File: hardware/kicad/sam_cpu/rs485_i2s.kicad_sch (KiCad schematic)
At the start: 22 parts, among them J27 J27 RS485 IN, J28 J28 I2S IN, J29 J29 RS485 OUT, J30 J30 LINE IN, U32 CA-IS2092VW

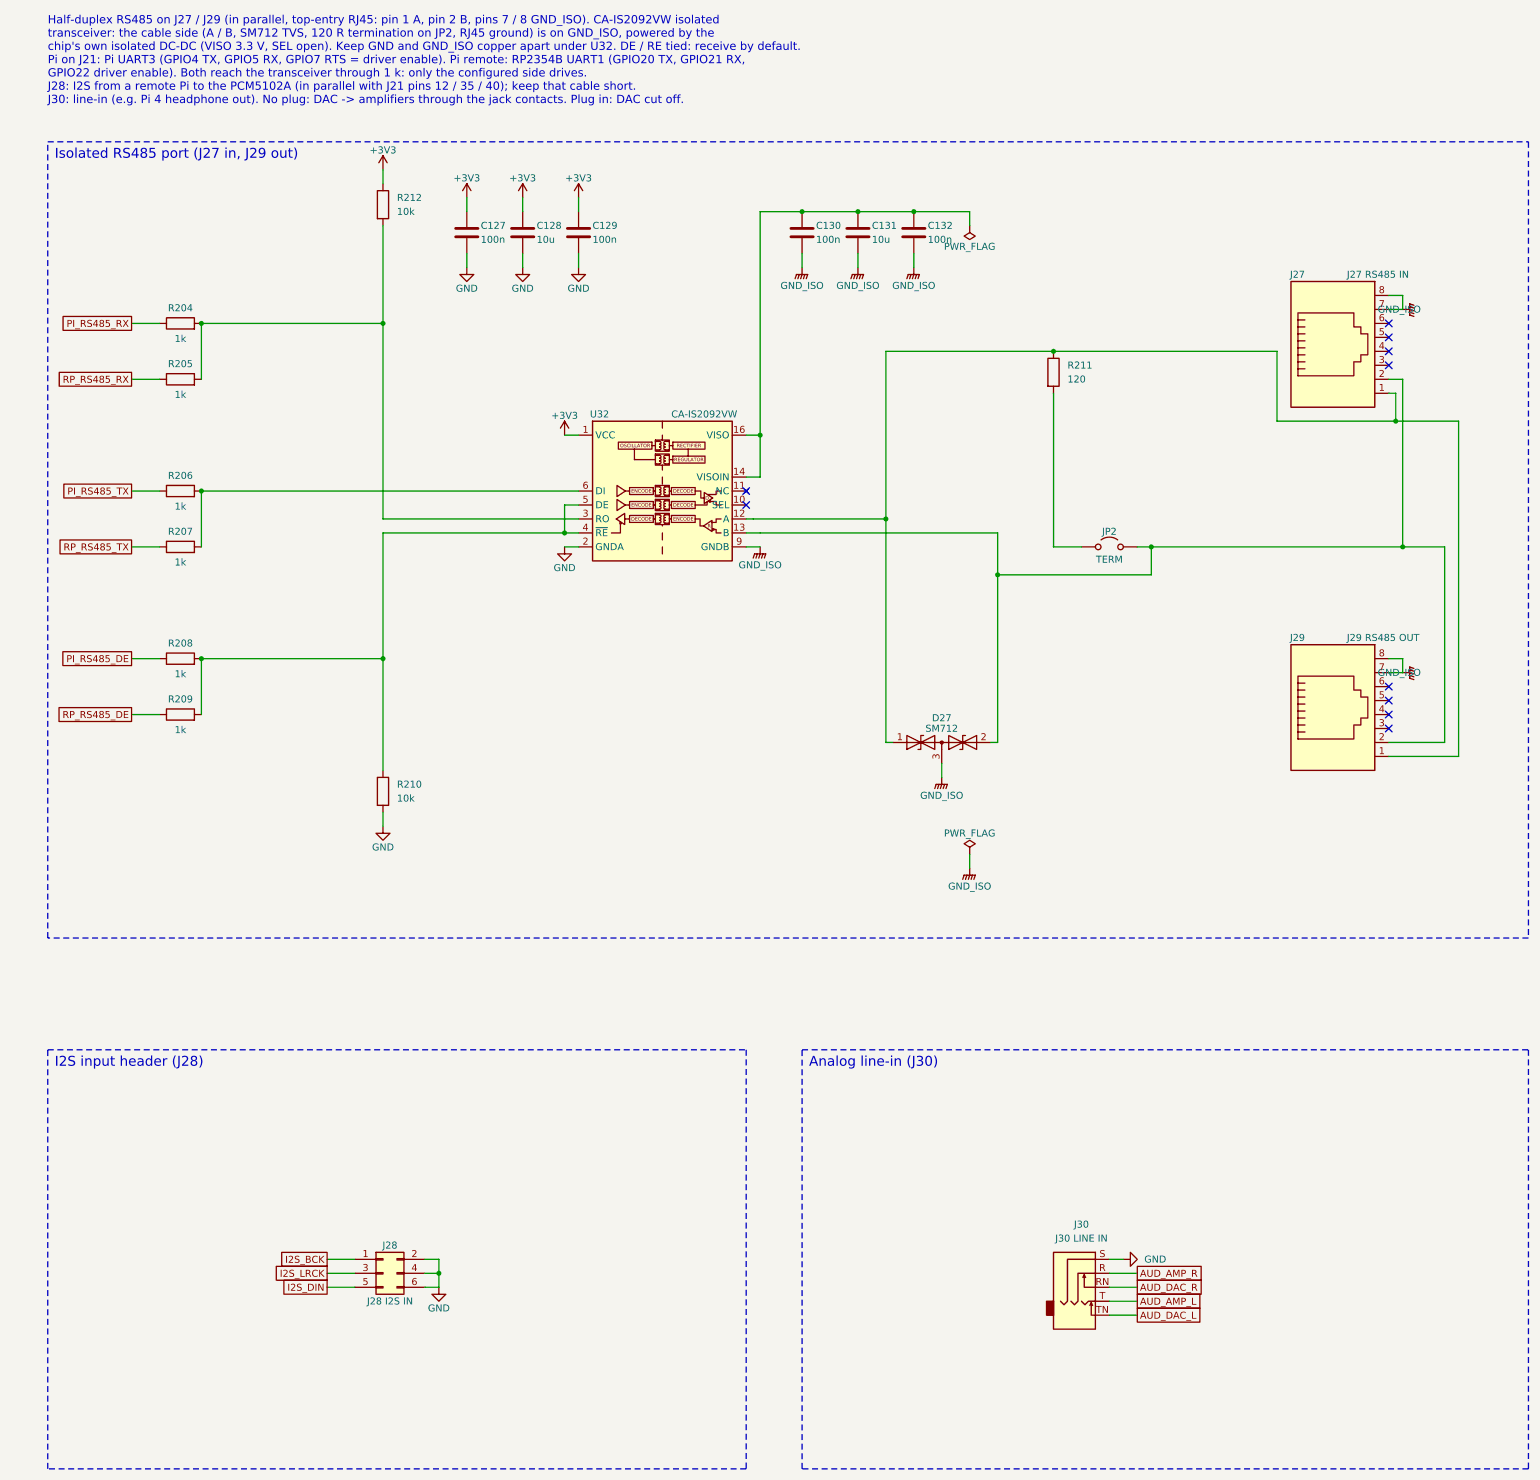
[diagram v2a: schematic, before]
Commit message: DIP switch block not loaded; larger schematic text
c30: SW3, R168-R175, U14 and C93 flagged DNP (schematic and board).
c31: schematic text 1.27 -> 1.6 mm (pins 1.5 mm), intersheet refs moved out.

Co-Authored-By: Claude Opus 5.5 (1M context) <noreply@anthropic.com>
Claude-Session: https://claude.ai/code/session_01ExuDVoDDDHhVWjb8EwVzYb
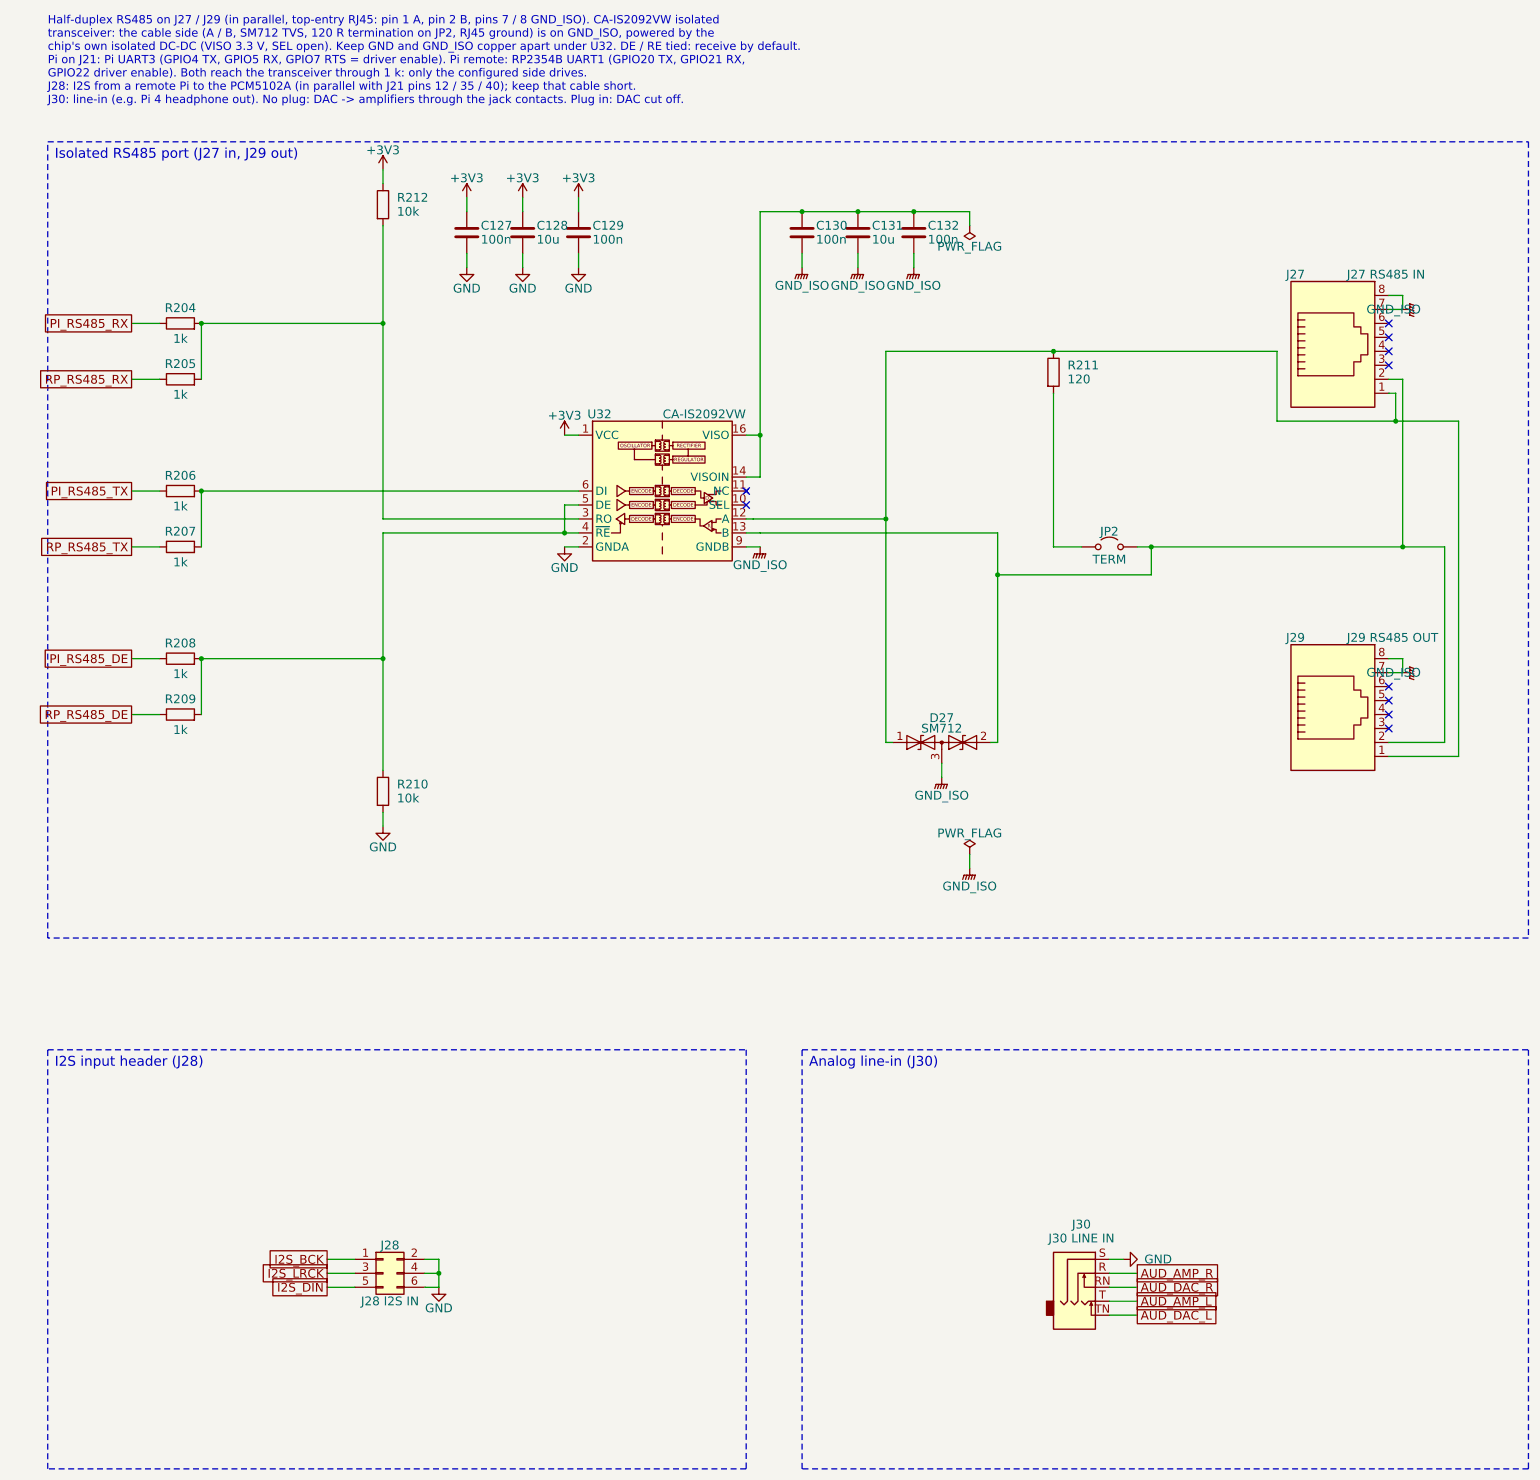
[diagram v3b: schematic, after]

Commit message: J19/J30 to JLCPCB-stocked parts (SH-U262-161N-4BVC11, PJ-393-7A)
J19 keeps the TYPE-C-31-M-12 pattern with the clone's longer rear shell slots.
J30 becomes the SMD PJ-393-7A switched stereo jack from the maker's drawing;
+12V, I2S_DIN, FRAME_SCK and the audio nets are rerouted around its pads.
Both footprints are added to sam_cpu.pretty. DRC and parity unchanged.

Co-Authored-By: Claude Opus 5.5 (1M context) <noreply@anthropic.com>
Claude-Session: https://claude.ai/code/session_01ExuDVoDDDHhVWjb8EwVzYb
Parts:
- J30: footprint Connector_Audio:Jack_3.5mm_CUI_SJ1-3535NG_Horizontal -> sam_cpu:Jack_3.5mm_PJ-393-7A_Horizontal
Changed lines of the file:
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@@
 			)
 		)
-		(property "Footprint" "Connector_Audio:Jack_3.5mm_CUI_SJ1-3535NG_Horizontal"
+		(property "Footprint" "sam_cpu:Jack_3.5mm_PJ-393-7A_Horizontal"
 			(at 203.2 243.84 0)
 			(hide yes)
